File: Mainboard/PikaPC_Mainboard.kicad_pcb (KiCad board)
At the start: 2 copper layers, 190.5 x 144.8 mm, 60 parts, among them J1 Conn_02x20_Odd_Even, J10 Conn_01x08, J11 Conn_01x08, J12 Conn_01x08, J13 Conn_01x08, J14 Conn_01x08, J15 Conn_01x08, J16 Conn_01x08, J17 Conn_01x08, J18 Conn_01x10, J19 Conn_02x05_Odd_Even, J2 Conn_02x20_Odd_Even, J3 Conn_02x20_Odd_Even, J4 Conn_02x20_Odd_Even, J5 Conn_01x18, J6 Conn_01x18, J7 Conn_01x18, J8 Conn_01x18, J9 Conn_01x08, SW1 SW_Push_DPDT, SW2 SW_Push, U1 PPC403GA, U10 74LVC245, U11 74LVC245, U12 GD75232N, U13 74LVC125, U14 MCP120-315GI/TO, U2 TE-822021-4, U3 SST39VF010, U4 74HCT244, U5 74HCT244, U6 74HCT244, U7 74LVC245, U8 74HCT32, U9 74LVC245, Y1 25M, Y2 7M3728

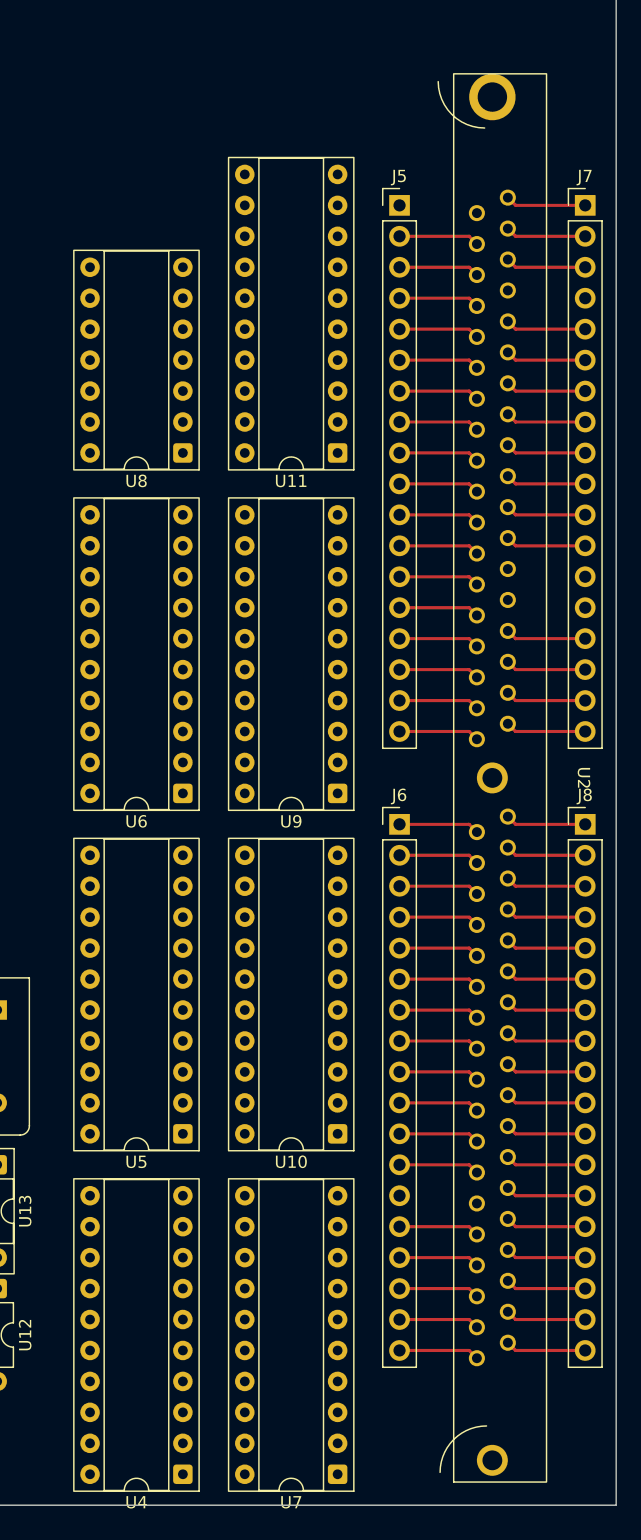
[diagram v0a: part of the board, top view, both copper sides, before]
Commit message: Change from 72-pin SIMM to SRAM
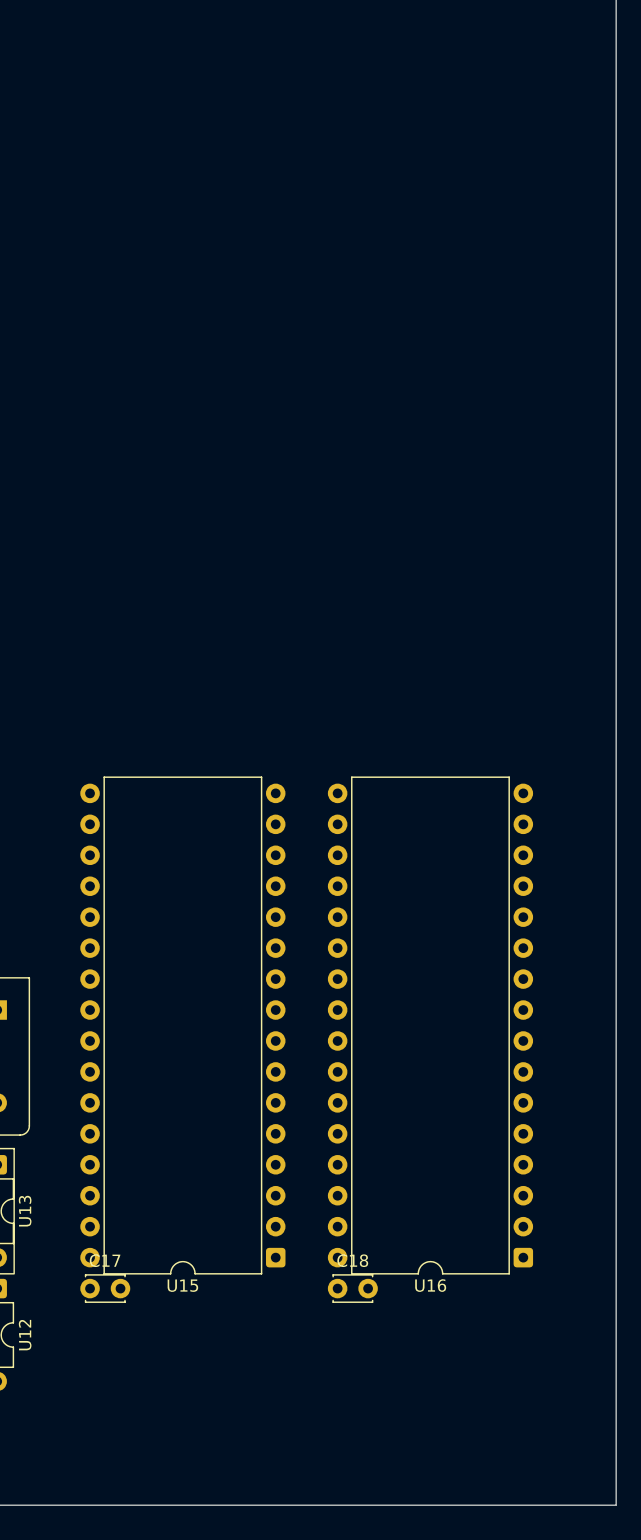
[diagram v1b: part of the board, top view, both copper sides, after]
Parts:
- removed J5, J6, J7, J8: Conn_01x18, Connector_PinHeader_2.54mm:PinHeader_1x18_P2.54mm_Vertical
- removed U10, U11, U7, U9: 74LVC245, Package_DIP:DIP-20_W7.62mm_Socket
- removed U2: TE-822021-4, PikaPC:SIMM72
- removed U4, U5, U6: 74HCT244, Package_DIP:DIP-20_W7.62mm_Socket
- removed U8: 74HCT32, Package_DIP:DIP-14_W7.62mm_Socket
- added C17: 100nF, Capacitor_THT:C_Disc_D3.0mm_W2.0mm_P2.50mm, F.Cu at (218.4, 142.2)
- added C18: 100nF, Capacitor_THT:C_Disc_D3.0mm_W2.0mm_P2.50mm, F.Cu at (238.8, 142.2)
- added U15: AS6C4008-55PCN, Package_DIP:DIP-32_W15.24mm, F.Cu at (233.7, 139.7)
- added U16: AS6C4008-55PCN, Package_DIP:DIP-32_W15.24mm, F.Cu at (254.0, 139.7)
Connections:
- U1 pad 122: /A27 -> /~{WBE0}
- U1 pad 123: /A26 -> /~{WBE1}
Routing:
- net +5V: track 37.5 -> 17.7 mm
- net GND: track 314.8 -> 295.0 mm
- net /~{MEM-RAS0}: track 13.2 -> 0.00 mm
- net /~{MEM-RAS1}: track 13.2 -> 0.00 mm
- net /MEM-A1: track 6.61 -> 0.00 mm
- net /MEM-A8: track 6.61 -> 0.00 mm
- net /MEM-D31: track 6.61 -> 0.00 mm
- net /MEM-D13: track 6.61 -> 0.00 mm
- net /MEM-D10: track 6.61 -> 0.00 mm
- net /~{MEM-CAS2}: track 6.61 -> 0.00 mm
- net /MEM-PD1: track 6.61 -> 0.00 mm
- net /MEM-D8: track 6.61 -> 0.00 mm
- net /~{MEM-CAS0}: track 6.61 -> 0.00 mm
- net /MEM-D5: track 6.61 -> 0.00 mm
- net /MEM-D28: track 6.61 -> 0.00 mm
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
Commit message: Rename write strobes
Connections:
- J4 pad 1: /A27 -> /~{WBE0}
- J4 pad 4: /A26 -> /~{WBE1}
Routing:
- net /~{WBE0}: track 0.00 -> 19.8 mm
- net /A27: track 19.8 -> 0.00 mm
- net /~{WBE1}: track 0.00 -> 15.8 mm
- net /A26: track 15.8 -> 0.00 mm

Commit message: use 5V signalling for Rx & CTS
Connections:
- U12 pad 14: /COM-CTS-5v -> /COM-CTS
- U12 pad 17: /COM-Rx-5v -> /COM-Rx
- U13 pad 2: /COM-Rx-5v -> unconnected-(U13-Pad2)
- U13 pad 3: /COM-Rx -> unconnected-(U13-Pad3)
- U13 pad 5: /COM-CTS-5v -> unconnected-(U13-Pad5)
- U13 pad 6: /COM-CTS -> unconnected-(U13-Pad6)
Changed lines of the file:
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@@
 	(net 140 "unconnected-(Y1-EN-Pad1)")
 	(net 141 "unconnected-(Y2-EN-Pad1)")
-	(net 142 "/COM-CTS-5v")
-	(net 143 "/COM-Rx-5v")
+	(net 142 "unconnected-(U13-Pad5)")
+	(net 143 "unconnected-(U13-Pad2)")
 	(net 144 "-12V")
 	(net 145 "+12V")
@@
 	(net 165 "/COM0-Rx")
 	(net 166 "/LED_3V3")
+	(net 167 "unconnected-(U13-Pad6)")
+	(net 168 "unconnected-(U13-Pad3)")
 	(footprint "Capacitor_SMD:C_0805_2012Metric"
 		(layer "F.Cu")
@@
 			(layers "*.Cu" "*.Mask")
 			(remove_unused_layers no)
-			(net 142 "/COM-CTS-5v")
+			(net 30 "/COM-CTS")
 			(pinfunction "RY4")
 			(pintype "output")
@@
 			(layers "*.Cu" "*.Mask")
 			(remove_unused_layers no)
-			(net 143 "/COM-Rx-5v")
+			(net 20 "/COM-Rx")
 			(pinfunction "RY3")
 			(pintype "output")
@@
 			(layers "*.Cu" "*.Mask")
 			(remove_unused_layers no)
-			(net 143 "/COM-Rx-5v")
+			(net 143 "unconnected-(U13-Pad2)")
 			(pintype "input")
 		)
@@
 			(layers "*.Cu" "*.Mask")
 			(remove_unused_layers no)
-			(net 20 "/COM-Rx")
+			(net 168 "unconnected-(U13-Pad3)")
 			(pintype "tri_state")
 		)
@@
 			(layers "*.Cu" "*.Mask")
 			(remove_unused_layers no)
-			(net 142 "/COM-CTS-5v")
+			(net 142 "unconnected-(U13-Pad5)")
 			(pintype "input")
 		)
@@
 			(layers "*.Cu" "*.Mask")
 			(remove_unused_layers no)
-			(net 30 "/COM-CTS")
+			(net 167 "unconnected-(U13-Pad6)")
 			(pintype "tri_state")
 		)

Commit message: Keyboard/Mouse controller use '04/'07
- use tried & true 7404+7407 instead of discrete transistors
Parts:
- added C19: 47p, Capacitor_THT:C_Disc_D7.5mm_W5.0mm_P7.50mm, F.Cu at (343.7, 74.8)
- added C20: 47p, Capacitor_THT:C_Disc_D7.5mm_W5.0mm_P7.50mm, F.Cu at (343.7, 81.4)
- added C21: 47p, Capacitor_THT:C_Disc_D7.5mm_W5.0mm_P7.50mm, F.Cu at (343.7, 87.9)
- added C22: 47p, Capacitor_THT:C_Disc_D7.5mm_W5.0mm_P7.50mm, F.Cu at (343.7, 94.5)
- added C23: 100nF, Capacitor_THT:C_Disc_D3.0mm_W2.0mm_P2.50mm, F.Cu at (142.2, 45.7)
- added J5: DIN41612_03x32_C_Split, Connector_DIN:DIN41612_C_3x32_Female_Vertical_THT, F.Cu at (81.3, 20.3)
- added J6: Mini-DIN-6, Connector_PinHeader_2.54mm:PinHeader_2x03_P2.54mm_Vertical, F.Cu at (180.3, 12.7)
- added J7: Mini-DIN-6, Connector_PinHeader_2.54mm:PinHeader_2x03_P2.54mm_Vertical, F.Cu at (195.6, 12.7)
- added R10: 4k7, Resistor_THT:R_Axial_DIN0204_L3.6mm_D1.6mm_P2.54mm_Vertical, F.Cu at (337.9, 98.3)
- added R2: 10k, Resistor_THT:R_Axial_DIN0204_L3.6mm_D1.6mm_P2.54mm_Vertical, F.Cu at (337.9, 73.1)
- added R5: 10k, Resistor_THT:R_Axial_DIN0204_L3.6mm_D1.6mm_P2.54mm_Vertical, F.Cu at (337.9, 82.6)
- added R8: 10k, Resistor_THT:R_Axial_DIN0204_L3.6mm_D1.6mm_P2.54mm_Vertical, F.Cu at (337.9, 92.0)
- added R9: 10k, Resistor_THT:R_Axial_DIN0204_L3.6mm_D1.6mm_P2.54mm_Vertical, F.Cu at (337.9, 95.2)
- added U10: 74LS07, Package_DIP:DIP-14_W7.62mm_Socket, F.Cu at (114.3, 35.6)
- added U2: SN74LVC245A, Package_DIP:DIP-20_W7.62mm_Socket, F.Cu at (134.6, 66.0)
- added U4: SN74LVC245A, Package_DIP:DIP-20_W7.62mm_Socket, F.Cu at (106.7, 66.0)
- added U5: SN74LVC245A, Package_DIP:DIP-20_W7.62mm_Socket, F.Cu at (134.6, 78.7)
- added U6: SN74LVC245A, Package_DIP:DIP-20_W7.62mm_Socket, F.Cu at (106.7, 78.7)
- added U7: 8042 PS/2, Package_DIP:DIP-40_W15.24mm_Socket, F.Cu at (124.5, 30.5)
- added U8: ATF22V10C, Package_DIP:DIP-24_W7.62mm_Socket, F.Cu at (134.6, 53.3)
- added U9: 74LS04, Package_DIP:DIP-14_W7.62mm_Socket, F.Cu at (91.4, 35.6)
- added Y3: 14M31818, Oscillator:Oscillator_DIP-8, F.Cu at (137.2, 38.1)
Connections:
- net /A0 renamed /A0/~{WBE3}
- net /A1 renamed /A1/~{WBE2}
- U1 pad 146: /~{RAS0} -> /~{CS7}
- U1 pad 147: /~{RAS1} -> /~{CS6}
- U1 pad 148: /~{RAS2} -> /~{CS5}
- U1 pad 151: /~{RAS3} -> /~{CS4}
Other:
- board size 190.5 x 144.8 mm -> 190.5 x 147.3 mm

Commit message: Add vS3 ViRGE video & SD interface
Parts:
- removed J2, J3, J4: Conn_02x20_Odd_Even, Connector_PinHeader_2.54mm:PinHeader_2x20_P2.54mm_Vertical
- added C24: 100nF, Capacitor_THT:C_Disc_D3.0mm_W2.0mm_P2.50mm, F.Cu at (200.7, 33.0)
- added J8: Conn_01x06, Connector_PinHeader_2.54mm:PinHeader_1x06_P2.54mm_Vertical, F.Cu at (205.7, 17.8)
- added R11: 75R, Resistor_THT:R_Axial_DIN0204_L3.6mm_D1.6mm_P2.54mm_Vertical, F.Cu at (226.1, 147.3)
- added R12: 10k, Resistor_THT:R_Axial_DIN0204_L3.6mm_D1.6mm_P2.54mm_Vertical, F.Cu at (188.0, 33.0)
- added R13: 10k, Resistor_THT:R_Axial_DIN0204_L3.6mm_D1.6mm_P2.54mm_Vertical, F.Cu at (190.5, 33.0)
- added R14: 10k, Resistor_THT:R_Axial_DIN0204_L3.6mm_D1.6mm_P2.54mm_Vertical, F.Cu at (193.0, 33.0)
- added R15: 10k, Resistor_THT:R_Axial_DIN0204_L3.6mm_D1.6mm_P2.54mm_Vertical, F.Cu at (195.6, 33.0)
- added R16: 10k, Resistor_THT:R_Axial_DIN0204_L3.6mm_D1.6mm_P2.54mm_Vertical, F.Cu at (198.1, 33.0)
- added R3: 4k7, Resistor_THT:R_Axial_DIN0204_L3.6mm_D1.6mm_P2.54mm_Vertical, F.Cu at (182.9, 33.0)
- added R4: 147R, Resistor_THT:R_Axial_DIN0204_L3.6mm_D1.6mm_P2.54mm_Vertical, F.Cu at (185.4, 33.0)
- added R6: 75R, Resistor_THT:R_Axial_DIN0204_L3.6mm_D1.6mm_P2.54mm_Vertical, F.Cu at (231.1, 147.3)
- added R7: 75R, Resistor_THT:R_Axial_DIN0204_L3.6mm_D1.6mm_P2.54mm_Vertical, F.Cu at (228.6, 147.3)
- added U11: 86C325, Package_QFP:PQFP-208_28x28mm_P0.5mm, F.Cu at (175.3, 63.5)
- added U17: ATF1504, Package_LCC:PLCC-44_THT-Socket, F.Cu at (213.4, 22.9)
- added U18: T224162B, Package_SO:SOJ-44_10.16x28.575mm_P1.27mm, F.Cu at (247.7, 81.3)
- added U19: T224162B, Package_SO:SOJ-44_10.16x28.575mm_P1.27mm, F.Cu at (219.7, 81.3)
- added U20: T224162B, Package_SO:SOJ-44_10.16x28.575mm_P1.27mm, F.Cu at (247.7, 50.8)
- added U21: T224162B, Package_SO:SOJ-44_10.16x28.575mm_P1.27mm, F.Cu at (219.7, 50.8)
- C10, C11, C12, C13, C9: footprint Capacitor_THT:C_Disc_D7.5mm_W5.0mm_P7.50mm -> Capacitor_THT:C_Disc_D7.0mm_W2.5mm_P5.00mm
- C19, C20, C21, C22: footprint Capacitor_THT:C_Disc_D7.5mm_W5.0mm_P7.50mm -> Capacitor_THT:C_Disc_D3.0mm_W2.0mm_P2.50mm
- J1: value Conn_02x20_Odd_Even -> Conn_02x05_Odd_Even; footprint Connector_PinHeader_2.54mm:PinHeader_2x20_P2.54mm_Vertical -> Connector_PinHeader_2.54mm:PinHeader_2x05_P2.54mm_Vertical
- moved R10 233.6 mm to (109.2, 50.8), turned to 180 degrees
- moved C22 180.7 mm to (177.8, 22.9)
- moved C21 180.6 mm to (175.3, 22.9), turned to 180 degrees
- moved R8 175.8 mm to (175.3, 25.4), turned to 180 degrees
- moved R9 174.7 mm to (177.8, 25.4)
- moved C20 164.0 mm to (190.5, 22.9), turned to 180 degrees
- moved C19 159.4 mm to (193.0, 22.9)
- moved R5 158.1 mm to (190.5, 25.4), turned to 180 degrees
- moved R2 152.5 mm to (193.0, 25.4)
- moved C7 148.1 mm to (181.6, 116.8)
- moved C4 145.4 mm to (181.6, 128.3), turned to -45 degrees
- moved C3 145.4 mm to (181.6, 142.2)
- moved C12 144.0 mm to (182.9, 102.9), turned to 180 degrees
- moved C11 137.8 mm to (179.1, 157.5), turned to 90 degrees
- moved C5 137.1 mm to (167.6, 100.3), turned to 90 degrees
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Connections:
- net Net-(U10-Pad1) renamed /~{MSDO}
- net Net-(U10-Pad3) renamed /~{MSCO}
- net Net-(U10-Pad5) renamed /~{KBCO}
- net Net-(U10-Pad9) renamed /~{KBDO}
- net Net-(U7-KBCO) renamed /KBCO
- net Net-(U7-KBDO) renamed /KBDO
- net Net-(U7-MSCO) renamed /MSCO
- net Net-(U7-MSDO) renamed /MSDO
- net Net-(U7-~{KBD-INH}) renamed /~{KINH}
- J1 pad 1: /~{DMAR0} -> /Vid-R
- J1 pad 10: /~{Halt} -> GND
- J1 pad 3: /~{DMAR2} -> /Vid-G
- J1 pad 4: /~{DMAR1} -> GND
- J1 pad 5: /TCK -> /Vid-B
- J1 pad 6: /~{DMAR3} -> GND
- J1 pad 7: /TDI -> /Vid-H
- J1 pad 8: /TMS -> GND
- J1 pad 9: GND -> /Vid-V
- U10 pad 10: unconnected-(U10-Pad10) -> /~{Reset-5v}
- U10 pad 11: unconnected-(U10-Pad11) -> /~{Reset}
- U13 pad 1: GND -> /PDReady
- U13 pad 2: unconnected-(U13-Pad2) -> +3.3V
- U13 pad 3: unconnected-(U13-Pad3) -> /Ready
- U13 pad 4: GND -> /SDReady
- U13 pad 5: unconnected-(U13-Pad5) -> +3.3V
- U13 pad 6: unconnected-(U13-Pad6) -> /Ready
- U8 pad 22: /Ready -> /Ready-5v
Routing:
- net GND: track 295.0 -> 610.0 mm
- net +5V: track 17.7 -> 302.5 mm
- net (no net): track 0.00 -> 67.2 mm
- net /VMA7: track 0.00 -> 66.2 mm
- net /VMA5: track 0.00 -> 43.2 mm
- net /VMA4: track 0.00 -> 42.3 mm
- net /VMA0: track 0.00 -> 40.4 mm
- net /~{VMRAS0}: track 0.00 -> 37.9 mm
- net /~{VMOE}: track 0.00 -> 37.7 mm
- net /VMA2: track 0.00 -> 37.3 mm
- net /PD23: track 0.00 -> 31.7 mm
- net /VMA8: track 0.00 -> 30.6 mm
- net /VMA1: track 0.00 -> 30.5 mm
- net /~{VMWE}: track 0.00 -> 28.2 mm
- net /VMA3: track 0.00 -> 28.2 mm
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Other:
- outline, holes or cut-outs redrawn
